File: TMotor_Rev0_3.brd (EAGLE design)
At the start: 106.7 x 74.3 mm, 94 parts, among them J1 5015680507, J10 5015680207, J2 5015680507, J7 5015680207, J8 5015680207, J9 5015680207, Q1 IRLB8721PBFTO220H, Q2 IRLB8721PBFTO220H, Q3 IRLB8721PBFTO220H, Q4 IRLB8721PBFTO220H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

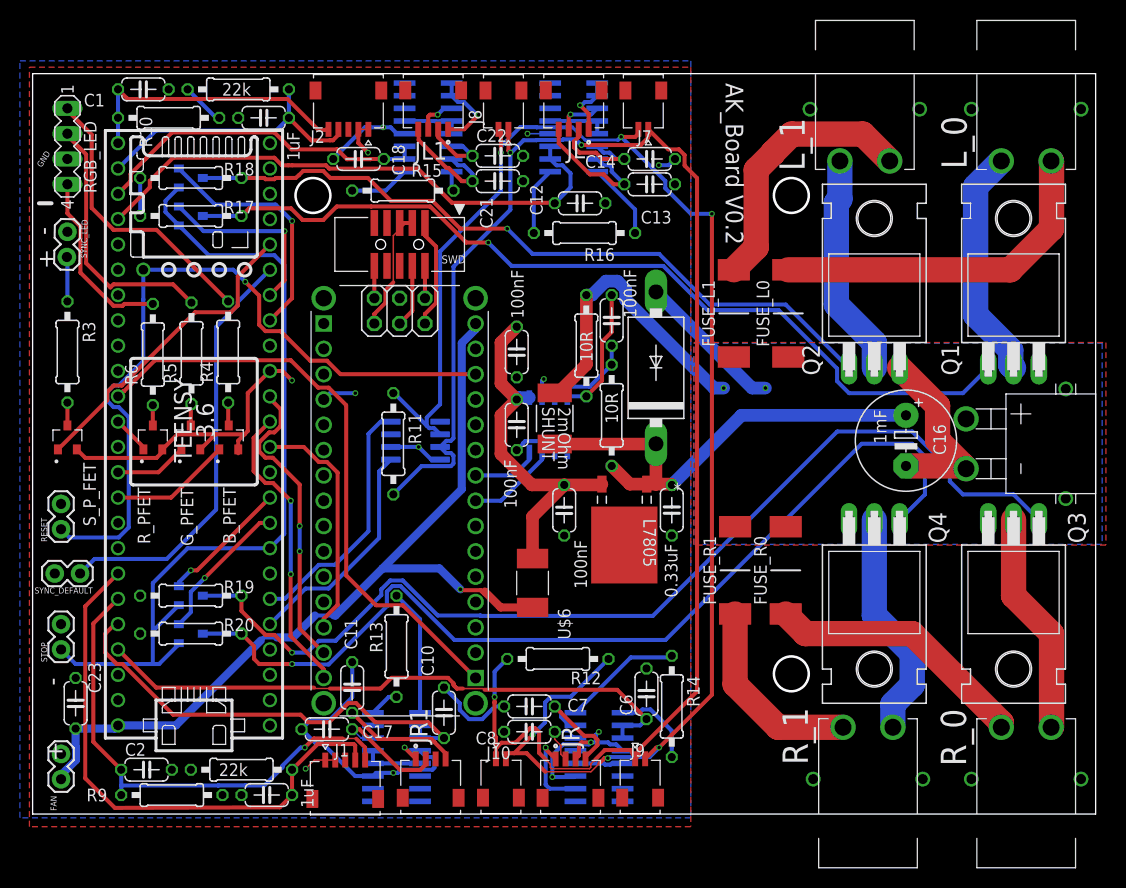
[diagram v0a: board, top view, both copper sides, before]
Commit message: updated board to use Teensy 4.1
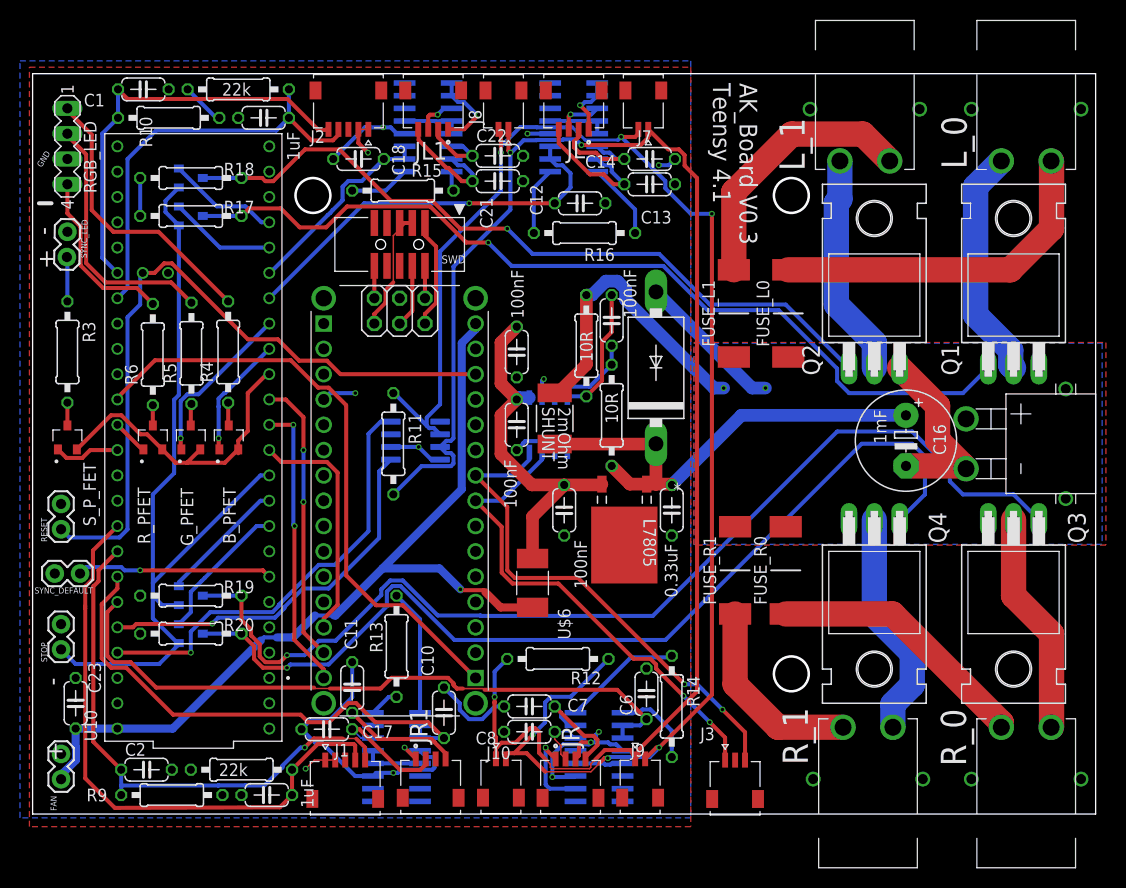
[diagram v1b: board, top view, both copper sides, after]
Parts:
- removed U$1: TEENSY_3.5/3.6_EXTERNAL_W/RESET, Teensy356:TEENSY_3.5/3.6_EXTERNAL_W/RESET
- added J3: 5015680307, SnapEDA-Library:MOLEX_5015680307
- added U10: DEV-16771, SnapEDA-Library:MODULE_DEV-16771
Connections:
- net 3.3V: now also U10.3.3V_1, U10.3.3V_2; no longer U$1.3V3
- net BLUE_LED_SIG: now also U10.24; no longer U$1.17/A3
- net CANRX: now also U10.23; no longer U$1.4/CANRX
- net CANTX: now also U10.22; no longer U$1.3/CANTX
- net FSR_HEEL_L: now also U10.38; no longer U$1.33/A14
- net FSR_HEEL_R: now also U10.19; no longer U$1.21/A7
- net FSR_TOE_L: now also U10.39; no longer U$1.34/A15
- net FSR_TOE_R: now also U10.18; no longer U$1.20/A6
- net GND: now also U10.GND1, U10.GND2, U10.GND3; no longer U$1.AGND, U$1.GND, U$1.GND2
- net GREEN_LED_SIG: now also U10.25; no longer U$1.16/A2
- net L_0_ENABLE: now also U10.28; no longer U$1.26
- net L_1_ENABLE: now also U10.29; no longer U$1.25
- net MISO: now also U10.11; no longer U$1.11/MOSI
- net MOSI: now also U10.12; no longer U$1.12/MISO
- net NANO_CS: now also U10.10; no longer U$1.10/CS
- net RED_LED_SIG: now also U10.14; no longer U$1.14/A0
- net RESET: now also U10.ON/OFF; no longer U$1.RESET
- net R_0_ENABLE: now also U10.8; no longer U$1.8
- net R_1_ENABLE: now also U10.7; no longer U$1.7
- net SCK: now also U10.13; no longer U$1.13/SCK
- net SCL0: now also J3.3
- net SDA0: now also J3.1
- net STOP: now also U10.9; no longer U$1.6
- net SYNC_DEFAULT: now also U10.5; no longer U$1.27
- net SYNC_SIG: now also U10.15; no longer U$1.28
- net TRQ_AMP_L: now also U10.26; no longer U$1.36/A17
- net TRQ_AMP_L1: now also U10.27; no longer U$1.35/A16
- net TRQ_AMP_R: now also U10.21; no longer U$1.23/A9
- net TRQ_AMP_R1: now also U10.20; no longer U$1.22/A8
- net VIN_PF: now also U10.VIN; no longer U$1.VIN
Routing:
- net SCL0: track 6.82 -> 51.1 mm, vias 0 -> 2
- net SDA0: track 9.15 -> 49.2 mm, vias 0 -> 2
- net SYNC_SIG: track 32.0 -> 6.65 mm
- net SYNC_DEFAULT: track 42.6 -> 19.6 mm, vias 0 -> 1
- net CANRX: track 25.2 -> 44.1 mm, vias 0 -> 1
- net TRQ_AMP_L: track 56.2 -> 40.2 mm, vias 0 -> 1
- net CANTX: track 22.9 -> 38.4 mm, vias 0 -> 1
- net TRQ_AMP_L1: track 34.1 -> 20.4 mm
- net L_1_ENABLE: track 24.4 -> 11.3 mm, vias 1 -> 0
- net FSR_TOE_L: track 28.8 -> 41.8 mm
- net GREEN_LED_SIG: track 7.30 -> 17.0 mm, vias 0 -> 1
- net FSR_HEEL_L: track 33.6 -> 42.5 mm
- net L_0_ENABLE: track 18.6 -> 10.8 mm, vias 1 -> 0
- net TRQ_AMP_R: track 60.8 -> 67.5 mm
- net TRQ_AMP_R1: track 46.4 -> 51.8 mm
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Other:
- board text added: "AK_Board V0.3 Teensy 4.1"
- board text removed: "AK_Board V0.2"
